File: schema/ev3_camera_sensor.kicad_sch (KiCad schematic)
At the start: 22 parts, among them J1 OV7675 B0070, J3 dry_cell_x2, J4 EV3_PORT_1, Q1 PMOS, Q2 INKA114AS1, Q3 INKA114AS1, Q4 INKA114AS1, SW1 RESET

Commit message: change LED chip
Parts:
- removed D3: OSTAMA5B31A, LED_SMD:LED_Cree-XHP50_3V_HighDensity, symbol Device:LED_GBAR
- removed D4: RED, symbol Device:LED
- removed J4: EV3_PORT_1, symbol Connector:Conn_01x06_Socket
- removed Q2, Q3, Q4: INKA114AS1, symbol Transistor_FET:Q_NMOS_GDS
- removed R4: 47Ω, symbol Device:R
- removed R5: 33Ω, symbol Device:R
- removed R6, R7: 680Ω, symbol Device:R
- removed SW1: RESET, Package_DFN_QFN:WDFN-10-1EP_3x3mm_P0.5mm_EP1.8x2.5mm, symbol Switch:SW_Push
- added J2: WS2812B, Package_CSP:Xilinx_CSG48_7.0x7.0mm_Layout7x7_P0.8mm, symbol Connector_Generic:Conn_02x02_Counter_Clockwise
- added J5: EV3_PORT_1, Relay_THT:Relay_SPDT_HJR-4102, symbol Connector:6P6C
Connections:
- net RGB_control_B is gone; now on net EV3_RX: A1.6 (GPIO4)
- net RGB_control_R is gone; now on net EV3_TX: A1.7 (GPIO5)
- net EV3_RX: now also J5.6 (RX); no longer A1.1 (GPIO0)
- net EV3_TX: now also J5.5 (TX); no longer A1.2 (GPIO1)
- net GND: now also J2.3 (Pin_3), J5.1 (ADC), J5.2 (GND)
- net RGB_control_G: no longer names the net of A1.5 (GPIO3)
- new net EV3_VCC: J2.1 (Pin_1), J5.4 (VCC)
- new net RGB_control: A1.1 (GPIO0), J2.4 (Pin_4)

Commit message: Update Schema
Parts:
- J1: value OV7675 B0070 -> OV7670
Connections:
- net OV7675_PDN: now also J1.18 (PDN); no longer J1.20 (PDN)
- net OV7675_PEN: now also J1.17 (RESET); no longer J1.19 (PEN)
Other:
- moved on the sheet: R1, R2
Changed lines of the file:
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@@
 	)
 	(junction
-		(at 236.22 137.16)
+		(at 236.22 134.62)
 		(diameter 0)
 		(color 0 0 0 0)
@@
 	)
 	(junction
-		(at 205.74 137.16)
+		(at 205.74 134.62)
 		(diameter 0)
 		(color 0 0 0 0)
@@
 	(wire
 		(pts
-			(xy 209.55 137.16) (xy 205.74 137.16)
-		)
-		(stroke
-			(width 0)
-			(type default)
-		)
-	)
-	(wire
-		(pts
-			(xy 236.22 149.86) (xy 236.22 147.32)
+			(xy 209.55 134.62) (xy 205.74 134.62)
+		)
+		(stroke
+			(width 0)
+			(type default)
+		)
+	)
+	(wire
+		(pts
+			(xy 236.22 147.32) (xy 236.22 144.78)
 		)
 		(stroke
@@
 	(wire
 		(pts
-			(xy 236.22 137.16) (xy 236.22 139.7)
+			(xy 236.22 134.62) (xy 236.22 137.16)
 		)
 		(stroke
@@
 	(wire
 		(pts
-			(xy 236.22 137.16) (xy 240.03 137.16)
-		)
-		(stroke
-			(width 0)
-			(type default)
-		)
-	)
-	(wire
-		(pts
-			(xy 233.68 137.16) (xy 236.22 137.16)
+			(xy 236.22 134.62) (xy 240.03 134.62)
+		)
+		(stroke
+			(width 0)
+			(type default)
+		)
+	)
+	(wire
+		(pts
+			(xy 233.68 134.62) (xy 236.22 134.62)
 		)
 		(stroke
@@
 	(wire
 		(pts
-			(xy 205.74 137.16) (xy 205.74 139.7)
+			(xy 205.74 134.62) (xy 205.74 137.16)
 		)
 		(stroke
@@
 	(wire
 		(pts
-			(xy 205.74 148.59) (xy 205.74 147.32)
+			(xy 205.74 146.05) (xy 205.74 144.78)
 		)
 		(stroke
@@
 	(wire
 		(pts
-			(xy 201.93 137.16) (xy 205.74 137.16)
+			(xy 201.93 134.62) (xy 205.74 134.62)
 		)
 		(stroke
@@
 	(global_label "3V3"
 		(shape input)
-		(at 205.74 148.59 270)
-		(fields_autoplaced yes)
-		(effects
-			(font
-				(size 1.27 1.27)
-			)
-			(justify right)
-		)
-		(property "Intersheetrefs" "${INTERSHEET_REFS}"
-			(at 205.74 155.0828 90)
+		(at 205.74 146.05 270)
+		(fields_autoplaced yes)
+		(effects
+			(font
+				(size 1.27 1.27)
+			)
+			(justify right)
+		)
+		(property "Intersheetrefs" "${INTERSHEET_REFS}"
+			(at 205.74 152.5428 90)
 			(hide yes)
 			(show_name no)
@@
 	(global_label "OV7675_PDN"
 		(shape output)
-		(at 240.03 137.16 0)
+		(at 240.03 134.62 0)
 		(fields_autoplaced yes)
 		(effects
@@
 		)
 		(property "Intersheetrefs" "${INTERSHEET_REFS}"
-			(at 255.1104 137.16 0)
+			(at 255.1104 134.62 0)
 			(hide yes)
 			(show_name no)
@@
 	(global_label "GND"
 		(shape passive)
-		(at 236.22 149.86 270)
-		(fields_autoplaced yes)
-		(effects
-			(font
-				(size 1.27 1.27)
-			)
-			(justify right)
-		)
-		(property "Intersheetrefs" "${INTERSHEET_REFS}"
-			(at 236.22 155.6044 90)
+		(at 236.22 147.32 270)
+		(fields_autoplaced yes)
+		(effects
+			(font
+				(size 1.27 1.27)
+			)
+			(justify right)
+		)
+		(property "Intersheetrefs" "${INTERSHEET_REFS}"
+			(at 236.22 153.0644 90)
 			(hide yes)
 			(show_name no)
@@
 	(global_label "OV7675_PEN"
 		(shape output)
-		(at 201.93 137.16 180)
-		(fields_autoplaced yes)
-		(effects
-			(font
-				(size 1.27 1.27)
-			)
-			(justify right)
-		)
-		(property "Intersheetrefs" "${INTERSHEET_REFS}"
-			(at 186.9706 137.16 0)
+		(at 201.93 134.62 180)
+		(fields_autoplaced yes)
+		(effects
+			(font
+				(size 1.27 1.27)
+			)
+			(justify right)
+		)
+		(property "Intersheetrefs" "${INTERSHEET_REFS}"
+			(at 186.9706 134.62 0)
 			(hide yes)
 			(show_name no)
@@
 			)
 		)
-		(property "Value" "OV7675 B0070"
+		(property "Value" "OV7670"
 			(at 221.742 110.998 0)
 			(show_name no)
@@
 		)
 		(pin "17"
-		)
-		(pin "19"
-		)
-		(pin "20"
 		)
 		(pin "8"
@@
 	(symbol
 		(lib_id "Device:R")
-		(at 205.74 143.51 0)
+		(at 205.74 140.97 0)
 		(unit 1)
 		(body_style 1)
@@
 		(fields_autoplaced yes)
 		(property "Reference" "R2"
+			(at 208.28 139.6999 0)
+			(show_name no)
+			(do_not_autoplace no)
+			(effects
+				(font
+					(size 1.27 1.27)
+				)
+				(justify left)
+			)
+		)
+		(property "Value" "10kΩ"
 			(at 208.28 142.2399 0)
 			(show_name no)
@@
 			)
 		)
-		(property "Value" "10kΩ"
-			(at 208.28 144.7799 0)
-			(show_name no)
-			(do_not_autoplace no)
-			(effects
-				(font
-					(size 1.27 1.27)
-				)
-				(justify left)
-			)
-		)
 		(property "Footprint" ""
-			(at 203.962 143.51 90)
+			(at 203.962 140.97 90)
 			(hide yes)
 			(show_name no)
@@
 		)
 		(property "Datasheet" ""
-			(at 205.74 143.51 0)
+			(at 205.74 140.97 0)
 			(hide yes)
 			(show_name no)
@@
 		)
 		(property "Description" "Resistor"
-			(at 205.74 143.51 0)
+			(at 205.74 140.97 0)
 			(hide yes)
 			(show_name no)
@@
 	(symbol
 		(lib_id "Device:R")
-		(at 236.22 143.51 0)
+		(at 236.22 140.97 0)
 		(unit 1)
 		(body_style 1)
@@
 		(fields_autoplaced yes)
 		(property "Reference" "R1"
+			(at 238.76 139.6999 0)
+			(show_name no)
+			(do_not_autoplace no)
+			(effects
+				(font
+					(size 1.27 1.27)
+				)
+				(justify left)
+			)
+		)
+		(property "Value" "10kΩ"
 			(at 238.76 142.2399 0)
 			(show_name no)
@@
 			)
 		)
-		(property "Value" "10kΩ"
-			(at 238.76 144.7799 0)
-			(show_name no)
-			(do_not_autoplace no)
-			(effects
-				(font
-					(size 1.27 1.27)
-				)
-				(justify left)
-			)
-		)
 		(property "Footprint" ""
-			(at 234.442 143.51 90)
+			(at 234.442 140.97 90)
 			(hide yes)
 			(show_name no)
@@
 		)
 		(property "Datasheet" ""
-			(at 236.22 143.51 0)
+			(at 236.22 140.97 0)
 			(hide yes)
 			(show_name no)
@@
 		)
 		(property "Description" "Resistor"
-			(at 236.22 143.51 0)
-			(hide yes)
-			(show_name no)
+			(at 236.22 140.97 0)
+			(hide yes)
+			(show_name no)

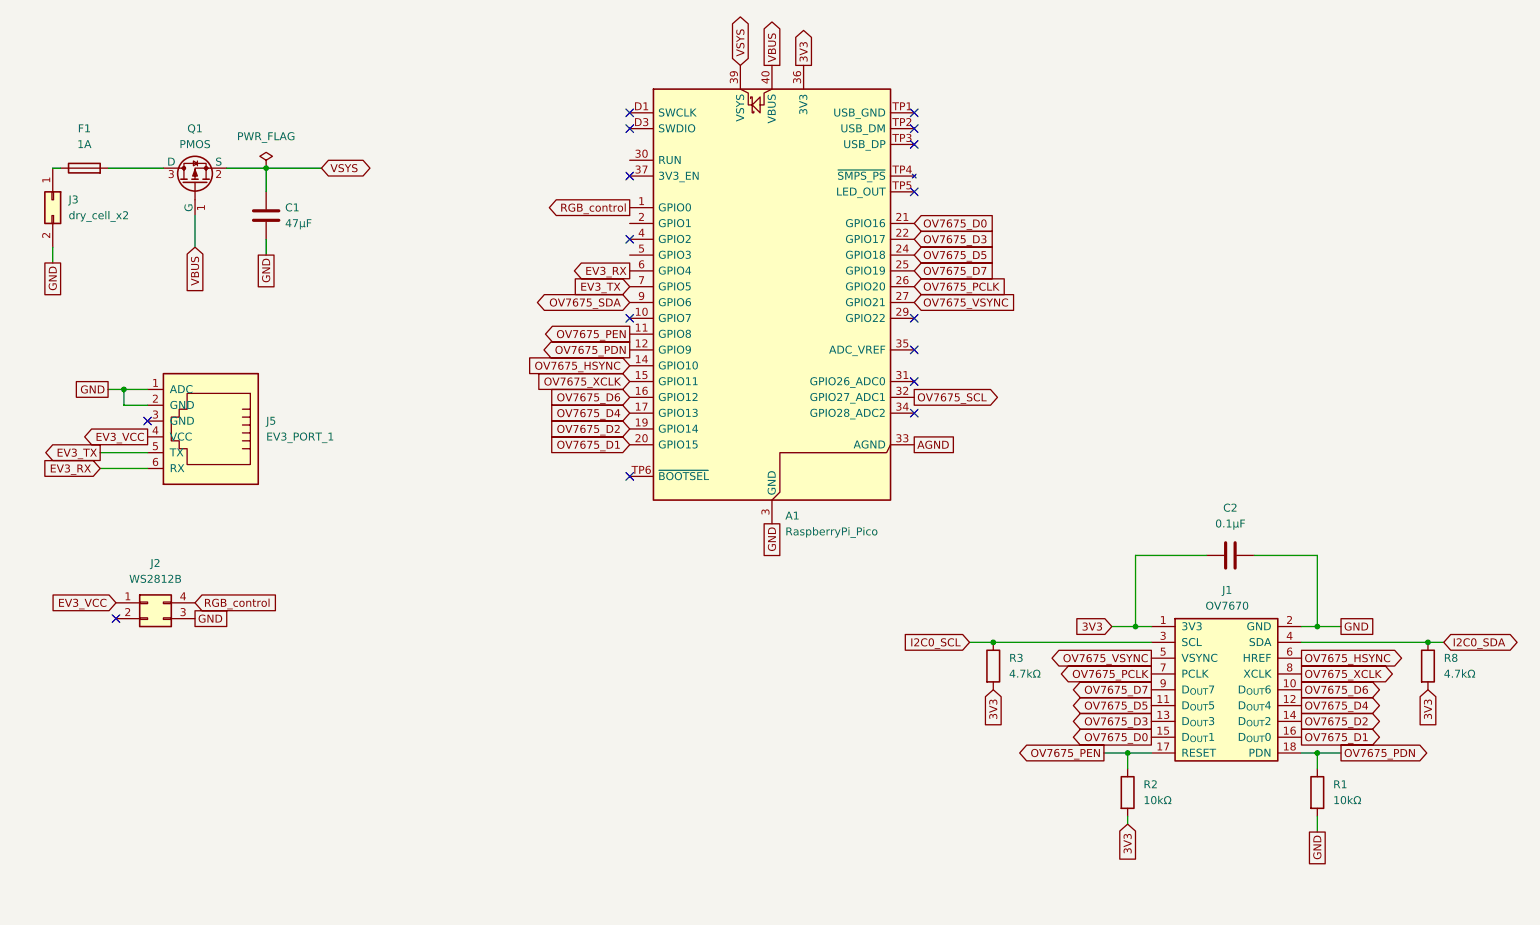
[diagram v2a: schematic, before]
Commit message: reflect removal of color led
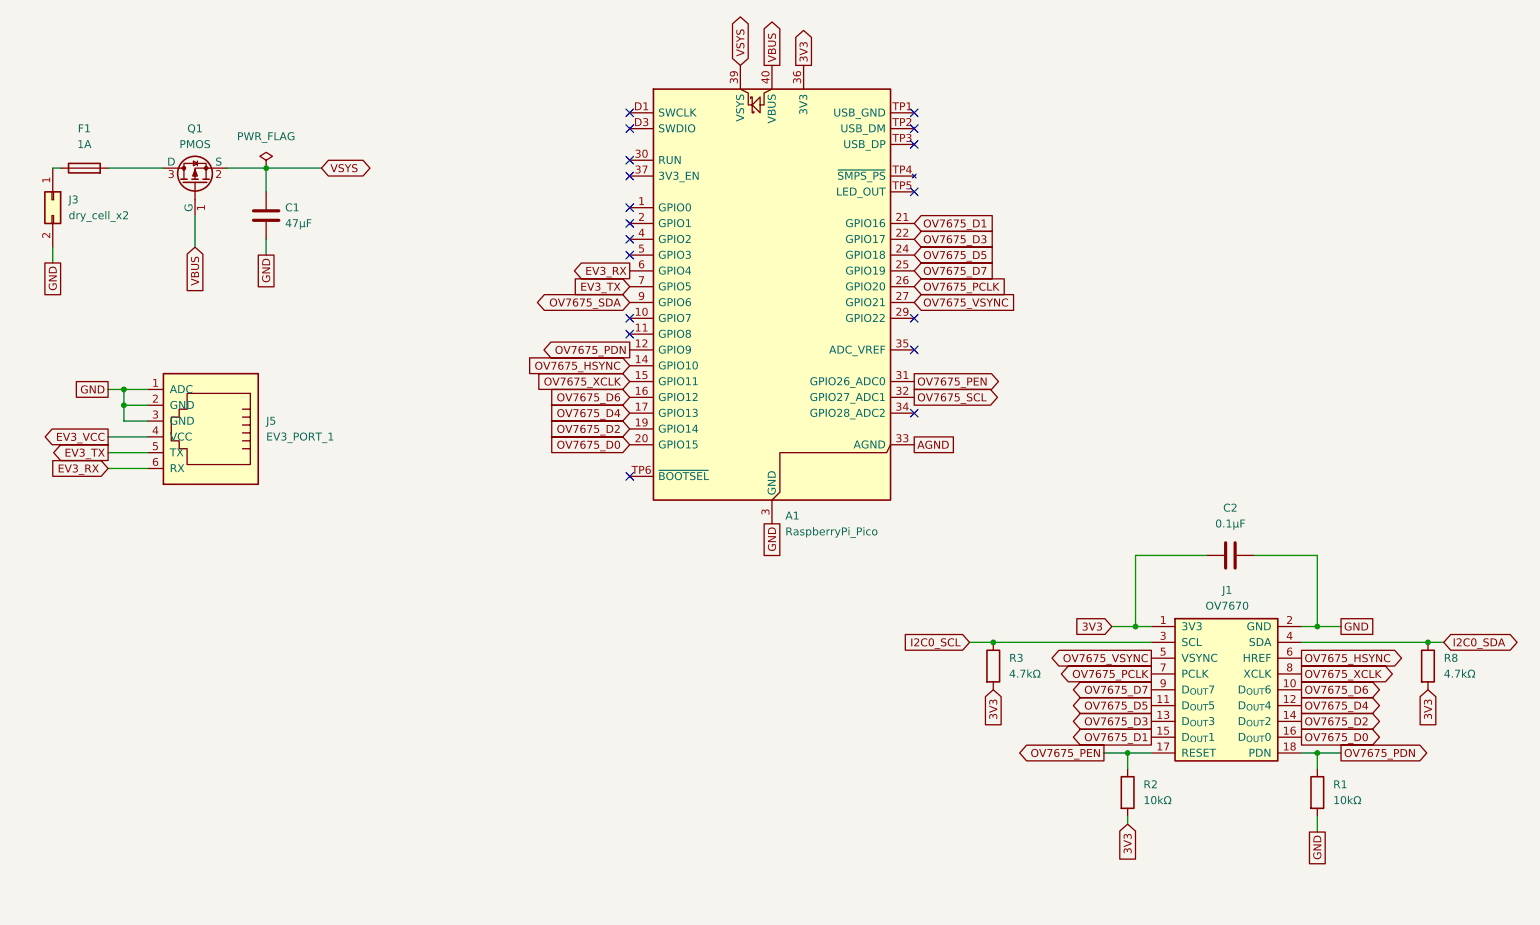
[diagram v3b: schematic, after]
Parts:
- removed J2: WS2812B, Package_CSP:Xilinx_CSG48_7.0x7.0mm_Layout7x7_P0.8mm, symbol Connector_Generic:Conn_02x02_Counter_Clockwise
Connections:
- net GND: now also J5.3 (GND)
- net OV7675_D0: now also A1.20 (GPIO15), J1.16 (D_{OUT}0); no longer A1.21 (GPIO16), J1.15 (D_{OUT}1)
- net OV7675_D1: now also A1.21 (GPIO16), J1.15 (D_{OUT}1); no longer A1.20 (GPIO15), J1.16 (D_{OUT}0)
- net OV7675_PEN: now also A1.31 (GPIO26_ADC0); no longer A1.11 (GPIO8)
- net RGB_control: no longer names the net of A1.1 (GPIO0)
- no-connect marks 16 -> 18
